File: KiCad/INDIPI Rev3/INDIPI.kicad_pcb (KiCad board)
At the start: 2 copper layers, 150 x 152 mm, 9 parts, among them J1 ADS1115, J16 Borneroa, J2 R PI GPIO 40, J3 MXP, J4 PMOD

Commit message: Rev3 complete revision and Gerbers generated
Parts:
- added MH6: MountingHole_2.5mm, MountingHole:MountingHole_2.5mm, F.Cu at (90.0, 30.0)
- added MH7: MountingHole_2.5mm, MountingHole:MountingHole_2.5mm, F.Cu at (109.0, 30.0)
- added MHR1: MountingHole_2.5mm, MountingHole:MountingHole_2.5mm, F.Cu at (48.0, 44.0)
- added MHR2: MountingHole_2.5mm, MountingHole:MountingHole_2.5mm, F.Cu at (106.0, 44.0)
- added MHR3: MountingHole_2.5mm, MountingHole:MountingHole_2.5mm, F.Cu at (48.0, 93.0)
- added MHR4: MountingHole_2.5mm, MountingHole:MountingHole_2.5mm, F.Cu at (106.0, 93.0)
- moved J16 2.00 mm to (43.0, 160.0)
- moved MH1 2.00 mm to (25.0, 25.0)
- moved MH2 2.00 mm to (165.0, 25.0)
- renumbered REF** to MH1, REF** to MH2, REF** to MH3, REF** to MH4
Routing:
- net Net-(J1-Pin_2): track 0.00 -> 219.9 mm, vias 0 -> 1
- net Net-(J1-Pin_1): track 0.00 -> 189.7 mm, vias 0 -> 1
- net Net-(J1-Pin_9): track 0.00 -> 170.3 mm, vias 0 -> 1
- net Net-(J1-Pin_10): track 0.00 -> 168.9 mm, vias 0 -> 1
- net Net-(J2-Pin_8): track 0.00 -> 138.5 mm, vias 0 -> 1
- net Net-(J2-Pin_10): track 0.00 -> 134.9 mm, vias 0 -> 1
- net Net-(J2-Pin_18): track 0.00 -> 131.2 mm, vias 0 -> 1
- net Net-(J1-Pin_7): track 0.00 -> 116.8 mm, vias 0 -> 1
- net Net-(J2-Pin_32): track 0.00 -> 116.1 mm, vias 0 -> 1
- net Net-(J1-Pin_8): track 0.00 -> 112.2 mm, vias 0 -> 1
- net Net-(J2-Pin_33): track 0.00 -> 110.2 mm, vias 0 -> 1
- net Net-(J2-Pin_12): track 0.00 -> 91.4 mm, vias 0 -> 1
- net Net-(J2-Pin_23): track 0.00 -> 87.3 mm, vias 0 -> 1
- net Net-(J2-Pin_19): track 0.00 -> 80.3 mm
- net Net-(J2-Pin_21): track 0.00 -> 74.2 mm
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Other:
- board size 150 x 152 mm -> 150 x 150 mm

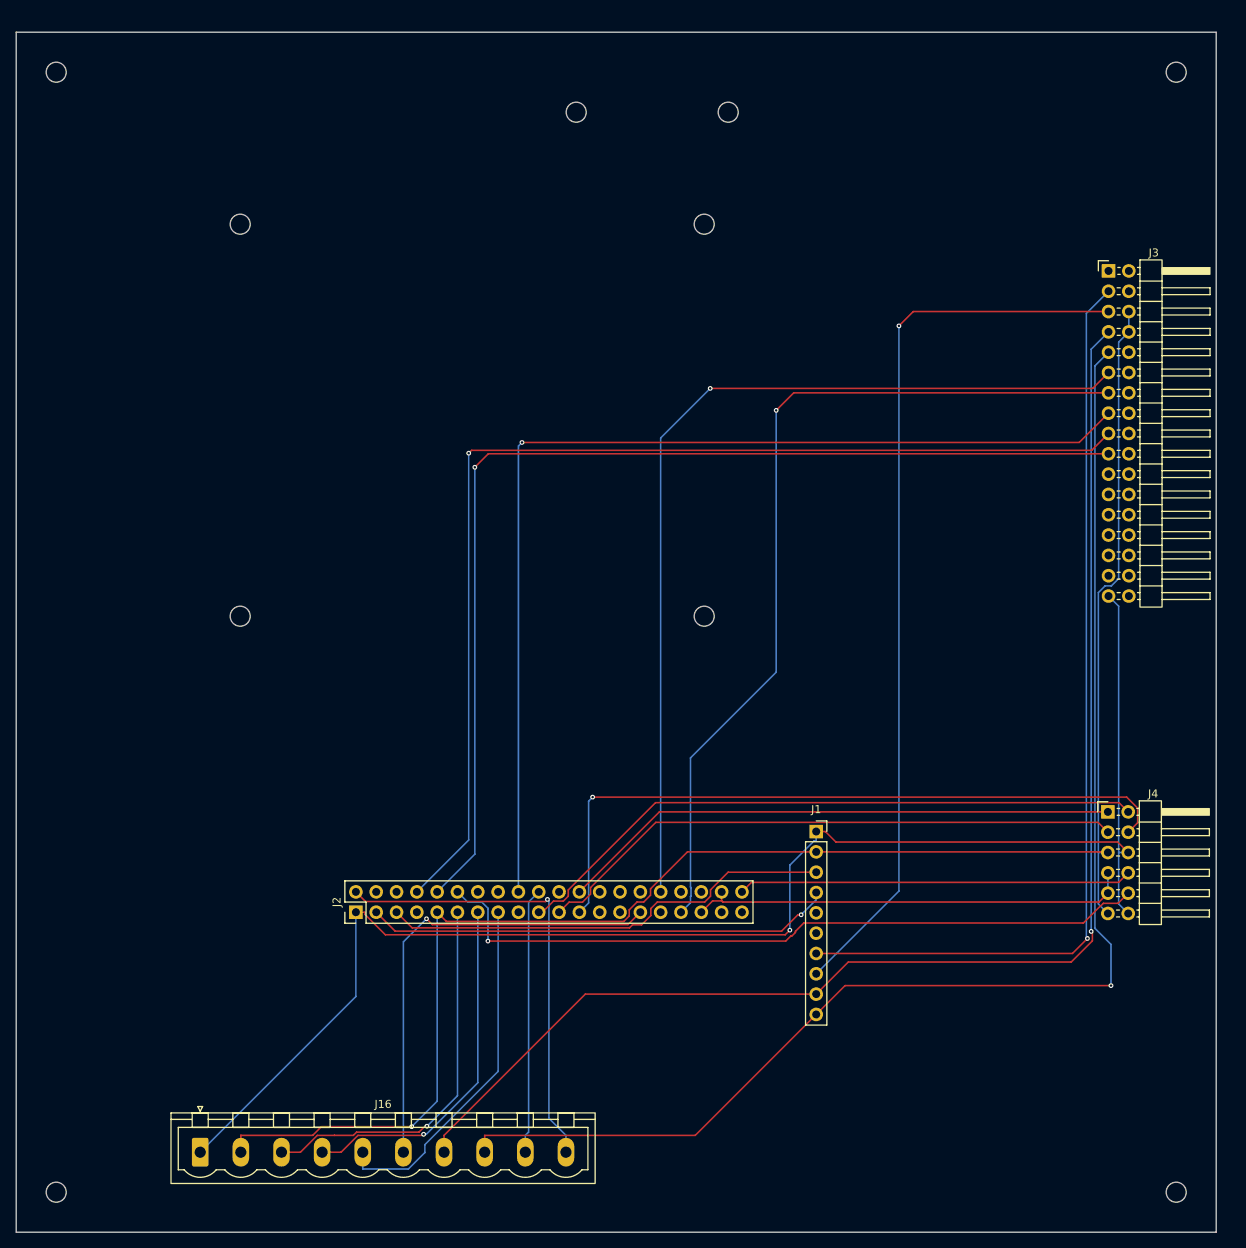
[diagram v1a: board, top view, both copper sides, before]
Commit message: Rev 3.1 - Decorations and hole adjustments
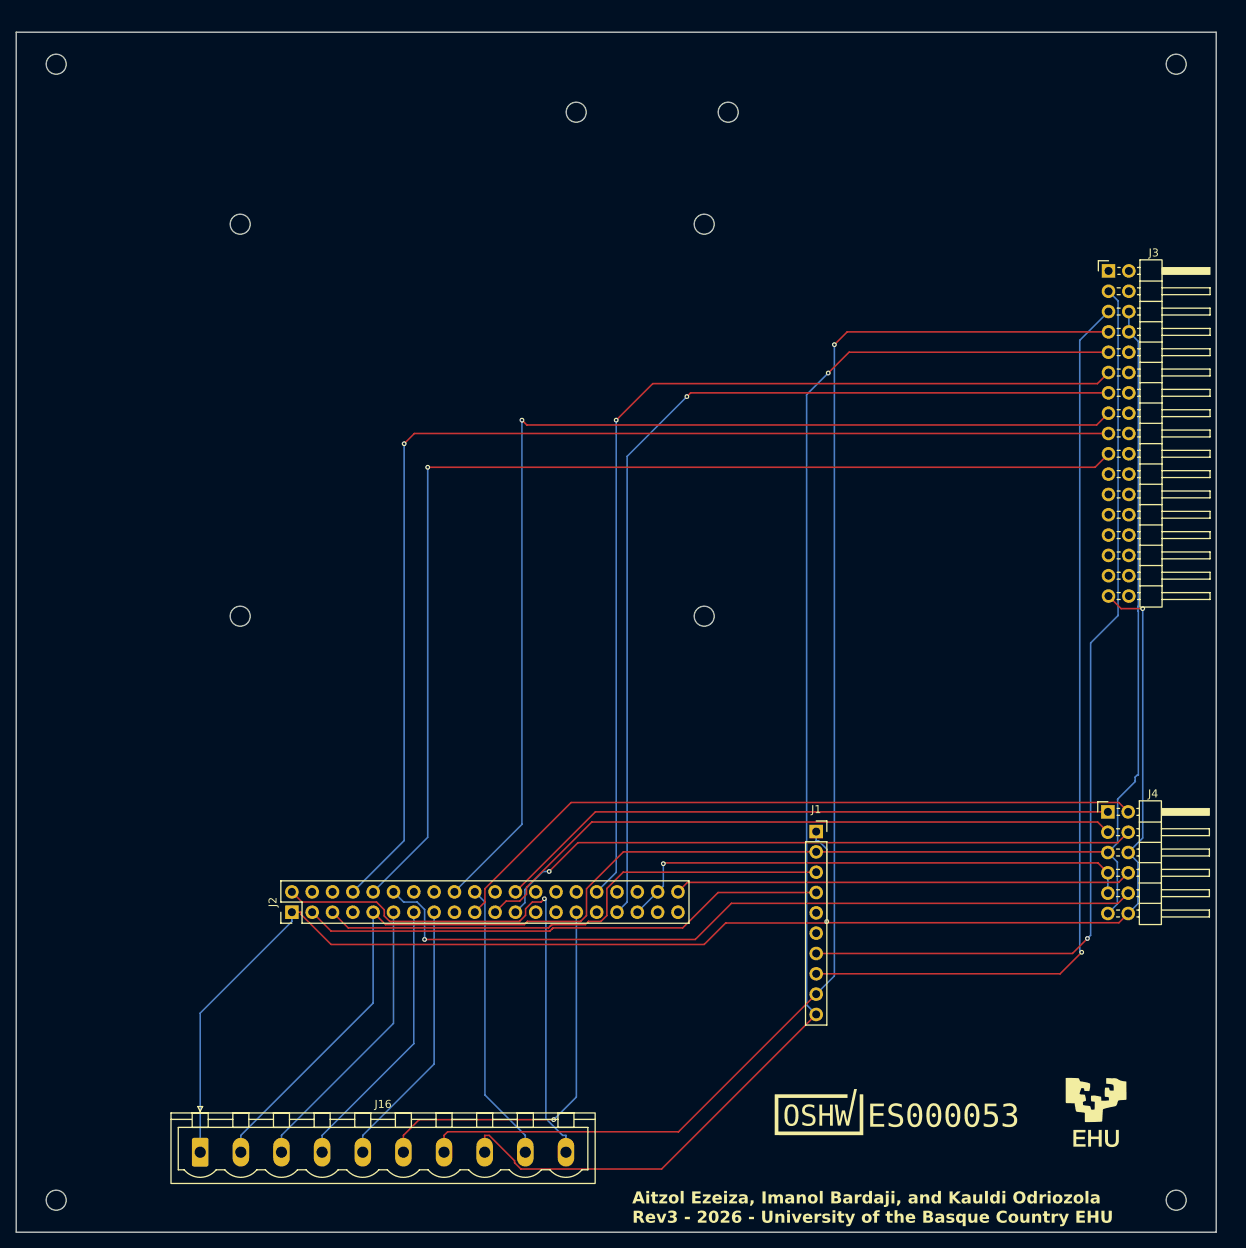
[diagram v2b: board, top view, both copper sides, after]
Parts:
- added EHU: LOGO, Custom Library:EHU_logotipo.txiki, F.Cu at (155.0, 155.0)
- added OSHWA: LOGO, Custom Library:OSHWA, F.Cu at (130.0, 155.0)
- moved J2 8.00 mm to (54.5, 130.0)
- moved MH1 1.00 mm to (25.0, 24.0)
- moved MH2 1.00 mm to (165.0, 24.0)
- moved MH3 1.00 mm to (25.0, 166.0)
- moved MH4 1.00 mm to (165.0, 166.0)
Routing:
- net Net-(J16-Pin_3): track 47.9 -> 35.8 mm, vias 1 -> 0
- net Net-(J16-Pin_10): track 57.1 -> 68.2 mm
- net Net-(J16-Pin_5): track 44.6 -> 33.7 mm
- net Net-(J2-Pin_33): track 110.2 -> 121.0 mm
- net Net-(J2-Pin_35): track 55.6 -> 66.1 mm, vias 0 -> 1
- net Net-(J1-Pin_1): track 189.7 -> 199.6 mm, vias 1 -> 2
- net Net-(J16-Pin_4): track 44.4 -> 34.7 mm, vias 1 -> 0
- net Net-(J1-Pin_3): track 57.1 -> 66.5 mm
- net Net-(J16-Pin_6): track 58.1 -> 48.8 mm
- net Net-(J2-Pin_8): track 138.5 -> 147.3 mm
- net Net-(J2-Pin_19): track 80.3 -> 88.8 mm
- net Net-(J2-Pin_21): track 74.2 -> 82.3 mm
- net Net-(J2-Pin_24): track 70.2 -> 78.2 mm
- net Net-(J2-Pin_40): track 49.3 -> 57.3 mm
- net Net-(J2-Pin_32): track 116.1 -> 124.0 mm
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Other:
- board text added: "Aitzol Ezeiza, Imanol Bardaji, and Kauldi Odriozola Rev3 - 2026 - University of the Basque Country EHU"
